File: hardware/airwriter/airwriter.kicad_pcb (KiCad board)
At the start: 2 copper layers, 52 x 78 mm, 64 parts, among them J1 USB-C 5V in, J2 Mini-DIN-8 to printer, J3 Bring-up USB/UART, J4 Mini-DIN-8 LocalTalk, J6 I2C / Qwiic, SW1 CONFIG/BOOT, SW2 MODE touch, U1 ESP32-S3-WROOM-1-N8R2, U2 MAX3490ESA+, U3 MAX3232ESE+, U4 AP7361C-33E, U5 USBLC6-2SC6, U6 SP3485EN-L, U7 PIC12F1840-I/P, U8 SP3485EN-L

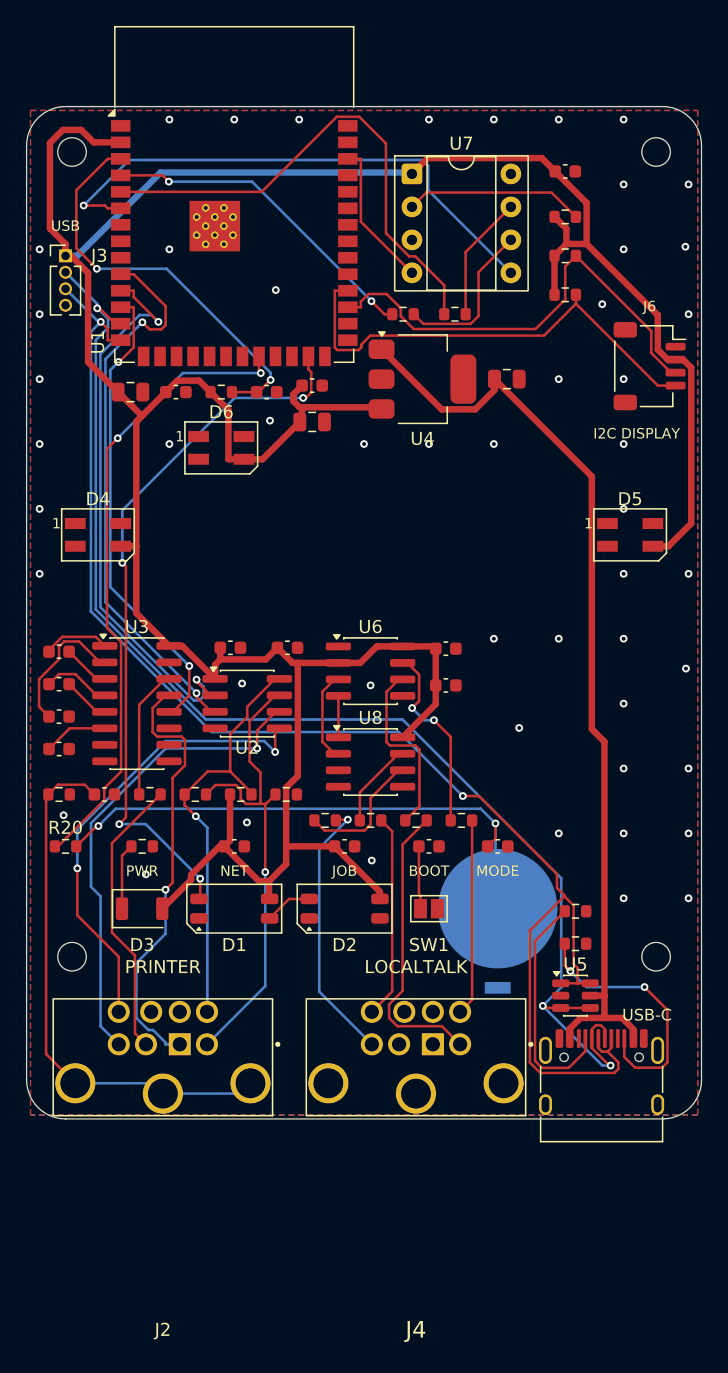
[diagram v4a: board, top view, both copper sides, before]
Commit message: Import the dithered cover artwork onto the back
Eight SVGs at 100 x 150mm, which is exactly 1.923x the board at the same aspect, so
they scale by 0.52 and mirror onto the back layers. Smallest cell lands at 0.455mm
and silk at 0.364mm, both clear of the fab floor.

Three departures from the artwork's README:

  It goes on B.*, not F.* -- the back is the display face, so everything mirrors.

  The *_gold_copper layer is not imported at all. The back is already a solid ground
  pour, so copper is everywhere; 503 separate islands would have shorted across
  traces. The mask openings alone give the gold, because the pour underneath is the
  copper. Same trick as the touch pad and the logo.

  The artwork's wordmark replaces the old rectangular logo window. They landed in
  the same place and a dithered wordmark beats a plain slab.

Order of operations is the whole game, and getting it wrong cost several passes.
Freerouting only sees keepouts that are separate single-outline zones: a zone holding
320 cell outlines exported to the DSN as ONE keepout, so the router drove straight
through the artwork. What works is reserve the wordmark with a single rectangle and
give each LED window its own zone -- sixteen keepouts reach the router and it honours
them -- then route, stitch, prune the stitching vias that landed in via-barred areas,
and only then filter the artwork against finished copper and emit it as rule areas
that bar copper pour only, so nothing needs re-routing.

Retention: wordmark FR4 282/293, grain FR4 23/27, gold 625/625 and 162/198. A further
141 cells gave way under silkscreen, mostly the long TashTalk credit across the top --
silk over exposed copper does not adhere. Move the credit if that band reads thin.

DRC is seven: the four known footprint mismatches, plus three silk-over-mask warnings
on the component side, which is inside the case. Drill floor 0.300mm. 983 mask
apertures and 60 silk cells on the back.
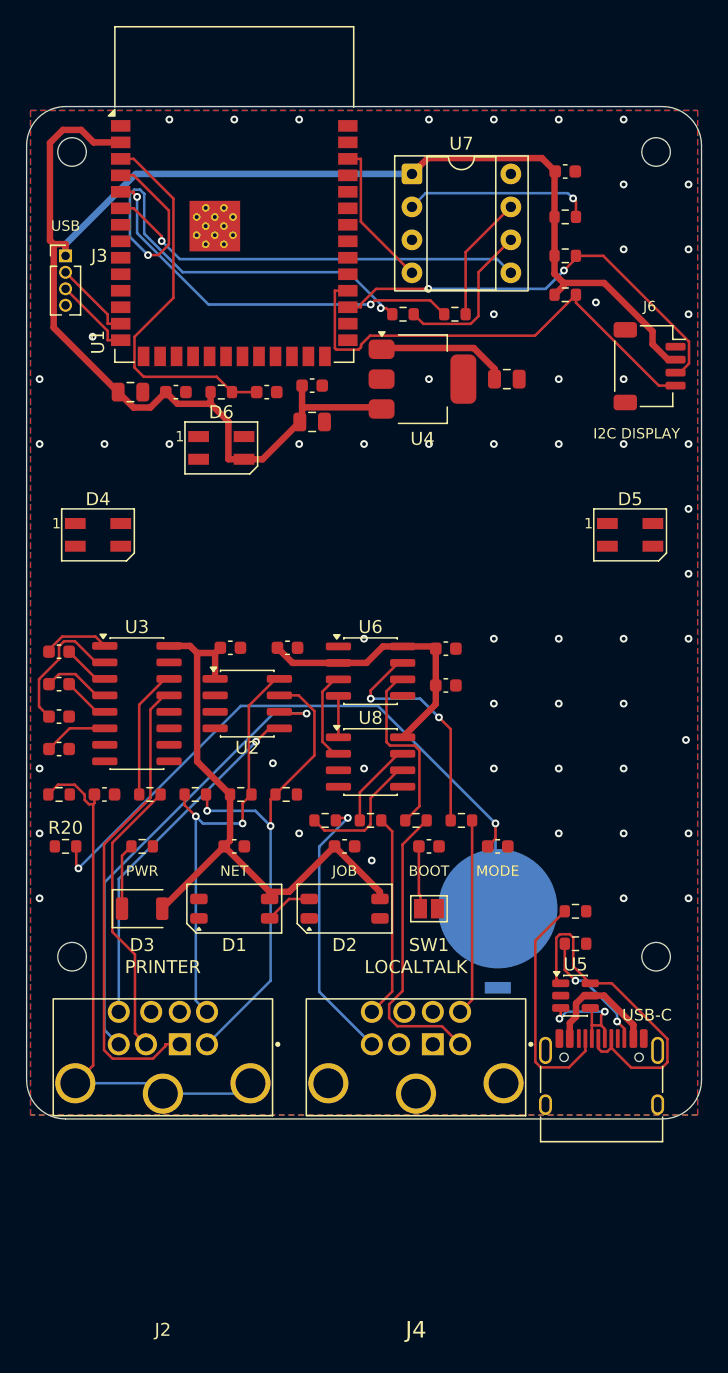
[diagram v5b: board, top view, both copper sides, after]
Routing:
- net /USB_DM: track 101.2 -> 16.3 mm, vias 3 -> 2
- net /USB_DP: track 110.2 -> 33.2 mm, vias 2 -> 0
- net /LED_DATA: track 55.3 -> 0.00 mm, vias 4 -> 0
- net /VBUS: track 73.0 -> 19.8 mm
- net /+3V3: track 242.5 -> 190.8 mm
- net /TOUCH_SENSE: track 48.9 -> 0.00 mm, vias 2 -> 0
- net /UART_RX: track 44.2 -> 0.00 mm, vias 2 -> 0
- net /UART_TX: track 43.0 -> 0.00 mm, vias 2 -> 0
- net /UART_CTS: track 36.3 -> 0.00 mm, vias 2 -> 0
- net /LT_UART_TX: track 25.4 -> 41.0 mm
- net /CC2: track 20.3 -> 9.59 mm
- net /LT_CTS: track 42.0 -> 32.3 mm
- net /BTN_MODE: track 42.6 -> 51.5 mm
- net /PR_RXD_P: track 35.7 -> 27.4 mm, vias 2 -> 1
- net /LT_UART_RX: track 39.0 -> 30.8 mm, vias 0 -> 2
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
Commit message: Drop the credit line and turn BOOT into a bullseye you can reach
The TashTalk credit ran the full width of B.Silkscreen and was eating a band of the
grain -- silk over exposed copper does not adhere, so every artwork cell beneath it
had to give way, 141 of them. The attribution still stands in the handoff, in SPEC.md
and in the licence; it does not need to be on the show face.

SW1 was SolderJumper-2_Open on the component side, which is inside the case. You
would have had to open the housing to reach a pad whose entire purpose is insurance
when USB will not enumerate. It is now airwriter:BootPads_Ring_D5mm on the back: a
2.2mm disc inside a 0.9mm ring, 0.5mm apart, both exposed ENIG. Bridge with tweezers.
Ø5mm against the MODE pad's Ø9.2mm so it reads as the secondary control, and the
concentric geometry answers MODE's arcs rather than fighting them.

artwork.py now carries the import, so the artwork is reproducible rather than a
one-off. It filters every cell against the copper actually on the board and emits
rule areas barring copper pour only, so it never forces a re-route. The order it
depends on is documented: strip, route, stitch, prune vias, artwork, refill.

Retention improved with the credit gone: wordmark FR4 280, grain 22, gold 776.

DRC is four, all the deliberate footprint mismatches. Drill floor 0.300mm.
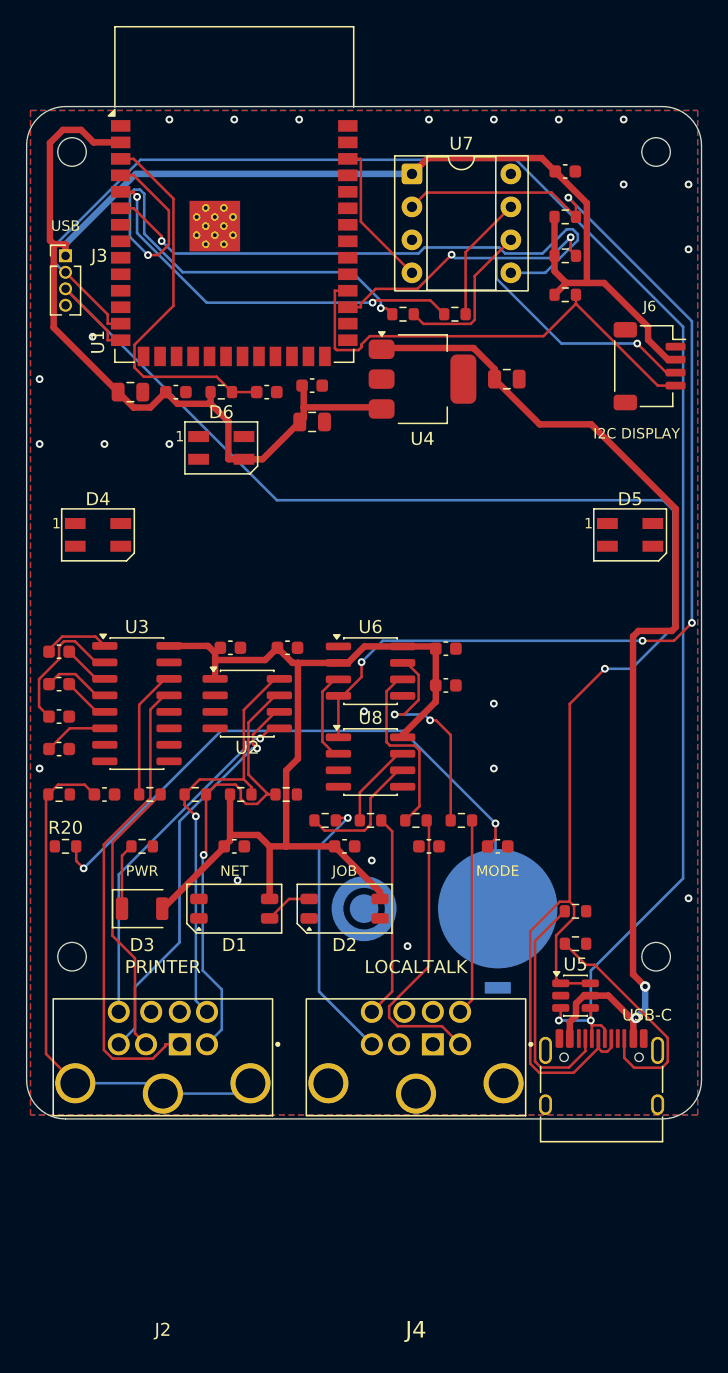
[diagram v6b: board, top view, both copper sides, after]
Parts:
- SW1: value CONFIG/BOOT -> BOOT bridge; footprint Jumper:SolderJumper-2_P1.3mm_Open_Pad1.0x1.5mm -> airwriter:BootPads_Ring_D5mm; moved to B.Cu
- moved SW1 5.00 mm to (126.0, 121.8)
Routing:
- net /USB_DM: track 16.3 -> 129.4 mm
- net /USB_DP: track 33.2 -> 127.5 mm, vias 0 -> 1
- net /LT_DATA: track 17.7 -> 85.7 mm, vias 1 -> 4
- net /VBUS: track 19.8 -> 81.1 mm, vias 0 -> 2
- net /+3V3: track 190.8 -> 205.2 mm
- net /LT_CTS: track 32.3 -> 44.9 mm
- net /CC2: track 9.59 -> 18.1 mm, vias 2 -> 0
- net /I2C_SDA: track 33.9 -> 39.7 mm, vias 2 -> 3
- net /BOOT_CFG: track 4.85 -> 0.00 mm
- net /PR_RXD_N: track 36.0 -> 31.4 mm
- net /PR_TXD_N: track 39.0 -> 36.8 mm, vias 2 -> 1
- net /BTN_MODE: track 51.5 -> 49.7 mm
- net /PR_TXD_P: track 33.9 -> 33.0 mm, vias 2 -> 1
- net /LT_Z: track 18.1 -> 17.4 mm
- net /GND: vias 55 -> 23
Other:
- board text removed: "BOOT"
- board text removed: "LocalTalk by TashTalk (lampmerchant) - CERN-OHL-S"

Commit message: Dither the two touch controls onto the cover's grid
The arcs and the bullseye were the only smooth geometry on a board whose whole back
is a dithered wordmark dissolving into grain. They read as hardware dropped onto the
artwork rather than as part of it.

Both are dithered now, on the cover's own 0.455mm cell grid, with density falling off
by radius. That fade is what makes a flat field read as a target instead of a blob,
and it echoes the way the grain dissolves above and below the wordmark. MODE is 150
cells over its 9.2mm disc; BOOT is a dense core inside a dithered ring at half the
diameter, so it still reads as the secondary control.

The copper did not change -- same solid disc for MODE, same disc-and-ring for BOOT --
so nothing needed re-routing. Only the soldermask moved, which is the same principle
the logo and the artwork already run on: mask carries the picture, copper carries the
function.

Both footprints come out of lib/gen_touchpads.py now, so grid, cell size and the
density curve are three numbers in one place rather than hand-drawn geometry. The
superseded arc and ring footprints are deleted.

DRC is four, all the deliberate footprint mismatches. Drill floor 0.300mm, 1258 mask
apertures on the back.
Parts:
- SW1: footprint airwriter:BootPads_Ring_D5mm -> airwriter:BootPads_Dither_D5mm
- SW2: footprint airwriter:TouchPad_Arcs_D9mm -> airwriter:TouchPad_Dither_D9mm

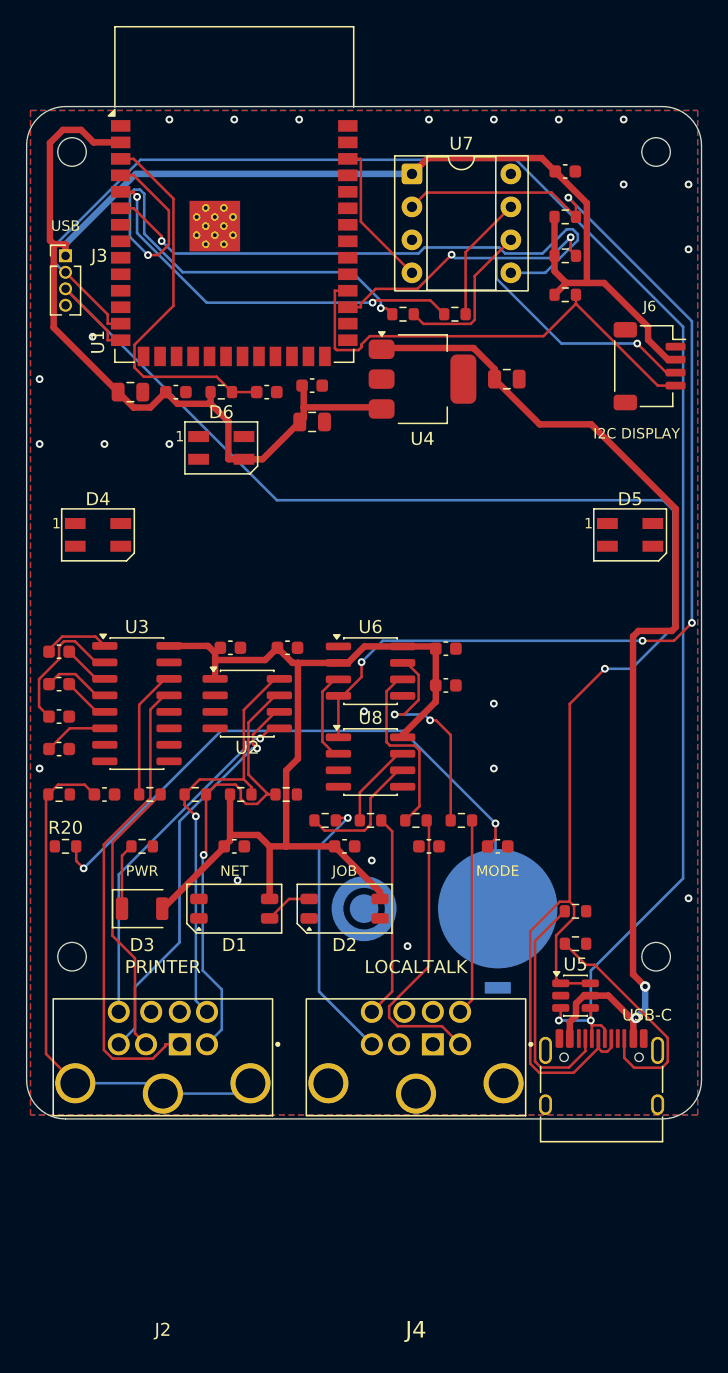
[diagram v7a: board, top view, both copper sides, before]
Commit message: Fix the routing regression the artwork introduced
The board has been carrying unrouted signals for several commits and I did not catch
it. kicad-cli reports pour islands and genuinely unrouted nets in the same
unconnected_items list, and route.py prints "Found N unconnected pads" for both, so a
board with UART_TX, UART_RX, UART_CTS, LED_DATA and USB_DP/DM disconnected still
showed four DRC violations and read as clean. At worst it was 16 real net breaks.
The router says so plainly if you read the whole line -- "(11 unrouted and 10
violations)" -- and a finished board has no unrouted clause at all.

The cause was the wordmark reserve: 49mm wide on a 52mm board, barring tracks on both
layers, leaving 0.5mm at one edge and 2.5mm at the other. Nothing could cross.

Fixed in two parts, both needed. The reserve is three separate blocks now, split at
natural gaps in the wordmark so traces have channels through the middle instead of
only round the ends. And it guards B.Cu only -- the visible face has to stay clear,
the component side does not. Letting F.Cu route under the wordmark is what took it
from nine unrouted to none. The cost is that a wordmark cell with a trace beneath it
stays dark rather than glowing, which in a dither is invisible; 198 of 293 cells
still light.

Two more things this turned up:

  Every rule area exports to Freerouting as a hard keepout whatever its tracks/vias
  settings say, so a pour-only guard still blocks the router. artwork.py now lays
  down the touch guard as well, after routing, for that reason.

  SW1 was sitting on top of D2. The BOOT pad is on B.Cu so the courtyard checks
  skipped it, but its centre via is through-hole and landed 1.5mm from a LED. Moved
  to (139.7, 111.3). Its ring is also open 60 degrees now and carries a via through
  the middle -- a fully enclosed centre pad cannot be routed to.

Board is fully routed. DRC is seven: four known footprint mismatches, three
silk-over-mask warnings on the component side. One unconnect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
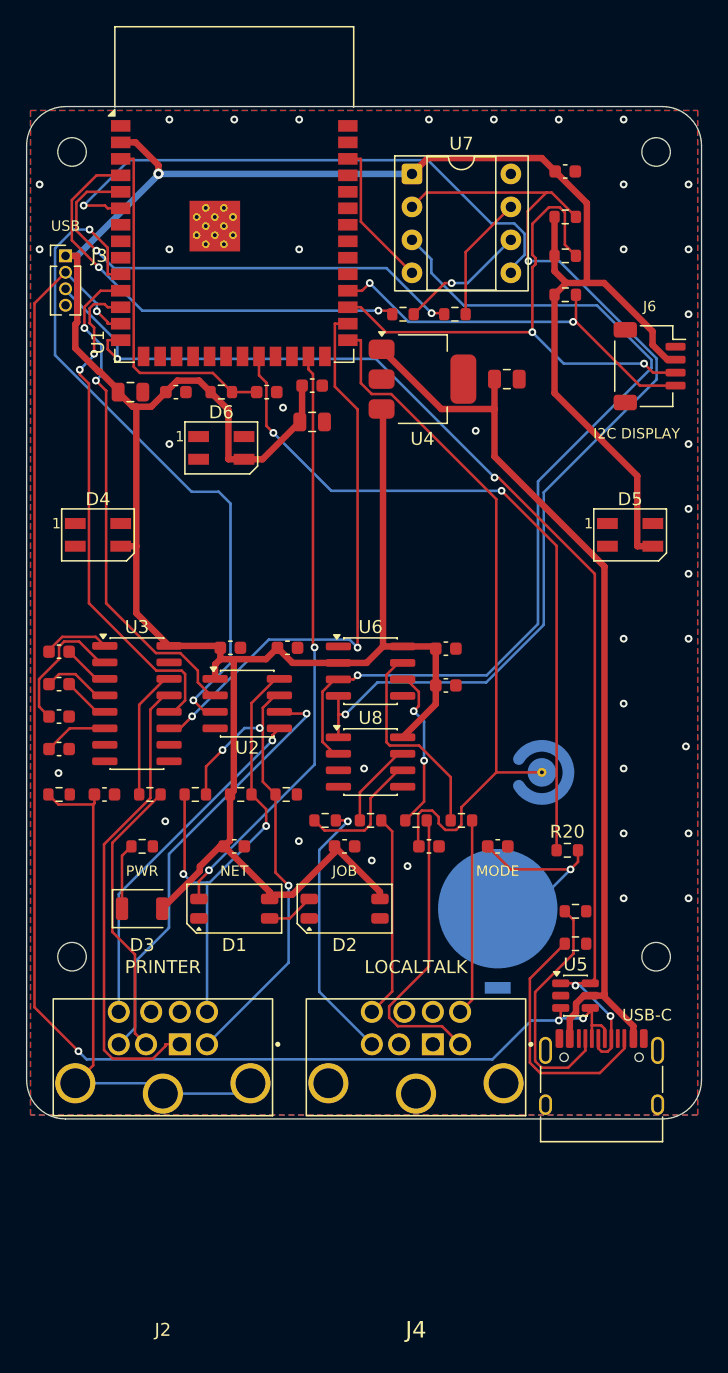
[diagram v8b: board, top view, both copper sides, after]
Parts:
- moved R20 38.7 mm to (141.7, 117.3)
- moved SW1 17.3 mm to (139.7, 111.3)
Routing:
- net /LT_DE: track 7.10 -> 71.1 mm, vias 0 -> 1
- net /TOUCH_SENSE: track 0.00 -> 55.2 mm, vias 0 -> 2
- net /BOOT_CFG: track 0.00 -> 55.2 mm
- net /UART_TX: track 0.00 -> 53.2 mm, vias 0 -> 2
- net /LED_DATA: track 0.00 -> 45.7 mm, vias 0 -> 2
- net /HSKI_DRV: track 0.00 -> 44.3 mm, vias 0 -> 2
- net /UART_CTS: track 0.00 -> 39.5 mm, vias 0 -> 2
- net /+3V3: track 205.2 -> 244.7 mm, vias 0 -> 1
- net /UART_RX: track 0.00 -> 39.0 mm, vias 0 -> 2
- net /BTN_MODE: track 49.7 -> 15.7 mm, vias 2 -> 1
- net /USB_DP: track 127.5 -> 95.7 mm, vias 1 -> 4
- net /USB_DM: track 129.4 -> 115.5 mm, vias 2 -> 4
- net /VBUS: track 81.1 -> 71.2 mm, vias 2 -> 0
- net /LT_DATA: track 85.7 -> 78.7 mm, vias 4 -> 2
- net /LT_UART_TX: track 41.1 -> 34.7 mm
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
